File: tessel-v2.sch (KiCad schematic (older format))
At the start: 0 parts

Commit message: io pins, jtag, cortex, high level pins
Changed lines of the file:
@@
 $EndSheet
 $Sheet
-S 6950 5000 2050 3550
+S 6950 5000 2050 4300
 U 548CB7C3
 F0 "I/O" 60
@@
 F9 "MT_WP" I L 6950 5600 60
 F10 "MT_HOLD" I L 6950 5700 60
-F11 "M1_SCL" I R 9000 6200 60
-F12 "M1_SDA" I R 9000 6300 60
-F13 "M1_CLK" I R 9000 6400 60
-F14 "M1_MISO" I R 9000 6500 60
-F15 "M1_MOSI" I R 9000 6600 60
-F16 "M1_G1/TX" I R 9000 6700 60
-F17 "M1_G2/RX" I R 9000 6800 60
-F18 "M1_G3" I R 9000 6900 60
-F19 "M2_SCL" I R 9000 7100 60
-F20 "M2_SDA" I R 9000 7200 60
-F21 "M2_CLK" I R 9000 7300 60
-F22 "M2_MISO" I R 9000 7400 60
-F23 "M2_MOSI" I R 9000 7500 60
-F24 "M2_G1/TX" I R 9000 7600 60
-F25 "M2_G2/RX" I R 9000 7700 60
-F26 "M2_G3" I R 9000 7800 60
-F27 "MT_SCL" I R 9000 5950 60
-F28 "MT_SDA" I R 9000 6050 60
+F11 "MT_SCL" I R 9000 5950 60
+F12 "MT_SDA" I R 9000 6050 60
+F13 "PORTA_SCL" I R 9000 6200 60
+F14 "PORTA_SDA" I R 9000 6300 60
+F15 "PORTA_CLK" I R 9000 6400 60
+F16 "PORTA_MISO" I R 9000 6500 60
+F17 "PORTA_MOSI" I R 9000 6600 60
+F18 "PORTA_G1/TX" I R 9000 6700 60
+F19 "PORTA_G2/RX" I R 9000 6800 60
+F20 "PORTA_G3" I R 9000 6900 60
+F21 "PORTB_SCL" I R 9000 7100 60
+F22 "PORTB_SDA" I R 9000 7200 60
+F23 "PORTB_CLK" I R 9000 7300 60
+F24 "PORTB_MISO" I R 9000 7400 60
+F25 "PORTB_MOSI" I R 9000 7500 60
+F26 "PORTB_G1/TX" I R 9000 7600 60
+F27 "PORTB_G2/RX" I R 9000 7700 60
+F28 "PORTB_G3" I R 9000 7800 60
+F29 "SAM_USB_DP" I R 9000 8000 60
+F30 "SAM_USB_DM" I R 9000 8100 60
+F31 "SWDIO" I R 9000 8250 60
+F32 "SWCLK" I R 9000 8350 60
+F33 "SAM_~RESET" I R 9000 8450 60
+F34 "MT_TWS" I L 6950 5950 60
+F35 "MT_~RESET" I L 6950 6050 60
+F36 "MT_TCLK" I L 6950 6150 60
+F37 "MT_TDO" I L 6950 6250 60
+F38 "MT_TDI" I L 6950 6350 60
+F39 "MT_RTCH" I L 6950 6450 60
 $EndSheet
+Wire Wire Line
+	9000 5150 10800 5150
+Wire Wire Line
+	10800 5150 10800 3650
+Wire Wire Line
+	10800 3650 13150 3650
+Wire Wire Line
+	9000 5250 10900 5250
+Wire Wire Line
+	10900 5250 10900 3750
+Wire Wire Line
+	10900 3750 13150 3750
+Wire Wire Line
+	9000 5500 10700 5500
+Wire Wire Line
+	10700 5500 10700 3050
+Wire Wire Line
+	10700 3050 13150 3050
+Wire Wire Line
+	9000 5600 10600 5600
+Wire Wire Line
+	10600 5600 10600 2850
+Wire Wire Line
+	10600 2850 13150 2850
+Wire Wire Line
+	9000 5700 10500 5700
+Wire Wire Line
+	10500 5700 10500 2950
+Wire Wire Line
+	10500 2950 13150 2950
+Wire Wire Line
+	9000 5800 10400 5800
+Wire Wire Line
+	10400 5800 10400 3150
+Wire Wire Line
+	10400 3150 13150 3150
+Wire Wire Line
+	9000 5950 10300 5950
+Wire Wire Line
+	10300 5950 10300 3450
+Wire Wire Line
+	10300 3450 13150 3450
+Wire Wire Line
+	9000 6050 10200 6050
+Wire Wire Line
+	10200 6050 10200 3350
+Wire Wire Line
+	10200 3350 13150 3350
+Wire Wire Line
+	9000 6200 13000 6200
+Wire Wire Line
+	13000 6200 13000 5350
+Wire Wire Line
+	13000 5350 13150 5350
+Wire Wire Line
+	9000 6300 12900 6300
+Wire Wire Line
+	12900 6300 12900 5250
+Wire Wire Line
+	12900 5250 13150 5250
+Wire Wire Line
+	9000 6400 12800 6400
+Wire Wire Line
+	12800 6400 12800 4850
+Wire Wire Line
+	12800 4850 13150 4850
+Wire Wire Line
+	9000 6500 12700 6500
+Wire Wire Line
+	12700 6500 12700 5050
+Wire Wire Line
+	12700 5050 13150 5050
+Wire Wire Line
+	9000 6600 12600 6600
+Wire Wire Line
+	12600 6600 12600 4750
+Wire Wire Line
+	12600 4750 13150 4750
+Wire Wire Line
+	9000 6700 12500 6700
+Wire Wire Line
+	12500 6700 12500 5550
+Wire Wire Line
+	12500 5550 13150 5550
+Wire Wire Line
+	9000 6800 12400 6800
+Wire Wire Line
+	12400 6800 12400 5650
+Wire Wire Line
+	12400 5650 13150 5650
+Wire Wire Line
+	9000 6900 12300 6900
+Wire Wire Line
+	12300 6900 12300 4100
+Wire Wire Line
+	12300 4100 13150 4100
+Wire Wire Line
+	9000 7100 13000 7100
+Wire Wire Line
+	13000 7100 13000 7750
+Wire Wire Line
+	13000 7750 13150 7750
+Wire Wire Line
+	9000 7200 12900 7200
+Wire Wire Line
+	12900 7200 12900 7650
+Wire Wire Line
+	12900 7650 13150 7650
+Wire Wire Line
+	9000 7300 12800 7300
+Wire Wire Line
+	12800 7300 12800 7350
+Wire Wire Line
+	12800 7350 13150 7350
+Wire Wire Line
+	9000 7400 12750 7400
+Wire Wire Line
+	12750 7400 12750 7150
+Wire Wire Line
+	12750 7150 13150 7150
+Wire Wire Line
+	9000 7500 12450 7500
+Wire Wire Line
+	12450 7500 12450 7250
+Wire Wire Line
+	12450 7250 13150 7250
+Wire Wire Line
+	9000 7600 12750 7600
+Wire Wire Line
+	12750 7600 12750 7950
+Wire Wire Line
+	12750 7950 13150 7950
+Wire Wire Line
+	9000 7700 12650 7700
+Wire Wire Line
+	12650 7700 12650 8050
+Wire Wire Line
+	12650 8050 13150 8050
+Wire Wire Line
+	9000 7800 12000 7800
+Wire Wire Line
+	12000 7800 12000 4200
+Wire Wire Line
+	12000 4200 13150 4200
+Wire Wire Line
+	4500 4150 9450 4150
+Wire Wire Line
+	9450 4150 9450 5500
+Connection ~ 9450 5500
+Wire Wire Line
+	4500 4250 9550 4250
+Wire Wire Line
+	9550 4250 9550 5600
+Connection ~ 9550 5600
+Wire Wire Line
+	4500 4350 9650 4350
+Wire Wire Line
+	9650 4350 9650 5700
+Connection ~ 9650 5700
+Wire Wire Line
+	4500 4450 6850 4450
+Wire Wire Line
+	6850 4450 6850 5600
+Wire Wire Line
+	6850 5600 6950 5600
+Wire Wire Line
+	4500 4550 6750 4550
+Wire Wire Line
+	6750 4550 6750 5700
+Wire Wire Line
+	6750 5700 6950 5700
+Wire Wire Line
+	4500 4650 6650 4650
+Wire Wire Line
+	6650 4650 6650 5500
+Wire Wire Line
+	6650 5500 6950 5500
 $Sheet
-S 13150 2700 2100 5500
+S 13150 2700 2100 6150
 U 548CB895
 F0 "COPROCESSOR" 60
@@
 F38 "GPIO_2_DAC" I L 13150 7050 60
 $EndSheet
-Wire Wire Line
-	9000 5150 10800 5150
-Wire Wire Line
-	10800 5150 10800 3650
-Wire Wire Line
-	10800 3650 13150 3650
-Wire Wire Line
-	9000 5250 10900 5250
-Wire Wire Line
-	10900 5250 10900 3750
-Wire Wire Line
-	10900 3750 13150 3750
-Wire Wire Line
-	9000 5500 10700 5500
-Wire Wire Line
-	10700 5500 10700 3050
-Wire Wire Line
-	10700 3050 13150 3050
-Wire Wire Line
-	9000 5600 10600 5600
-Wire Wire Line
-	10600 5600 10600 2850
-Wire Wire Line
-	10600 2850 13150 2850
-Wire Wire Line
-	9000 5700 10500 5700
-Wire Wire Line
-	10500 5700 10500 2950
-Wire Wire Line
-	10500 2950 13150 2950
-Wire Wire Line
-	9000 5800 10400 5800
-Wire Wire Line
-	10400 5800 10400 3150
-Wire Wire Line
-	10400 3150 13150 3150
-Wire Wire Line
-	9000 5950 10300 5950
-Wire Wire Line
-	10300 5950 10300 3450
-Wire Wire Line
-	10300 3450 13150 3450
-Wire Wire Line
-	9000 6050 10200 6050
-Wire Wire Line
-	10200 6050 10200 3350
-Wire Wire Line
-	10200 3350 13150 3350
-Wire Wire Line
-	9000 6200 13000 6200
-Wire Wire Line
-	13000 6200 13000 5350
-Wire Wire Line
-	13000 5350 13150 5350
-Wire Wire Line
-	9000 6300 12900 6300
-Wire Wire Line
-	12900 6300 12900 5250
-Wire Wire Line
-	12900 5250 13150 5250
-Wire Wire Line
-	9000 6400 12800 6400
-Wire Wire Line
-	12800 6400 12800 4850
-Wire Wire Line
-	12800 4850 13150 4850
-Wire Wire Line
-	9000 6500 12700 6500
-Wire Wire Line
-	12700 6500 12700 5050
-Wire Wire Line
-	12700 5050 13150 5050
-Wire Wire Line
-	9000 6600 12600 6600
-Wire Wire Line
-	12600 6600 12600 4750
-Wire Wire Line
-	12600 4750 13150 4750
-Wire Wire Line
-	9000 6700 12500 6700
-Wire Wire Line
-	12500 6700 12500 5550
-Wire Wire Line
-	12500 5550 13150 5550
-Wire Wire Line
-	9000 6800 12400 6800
-Wire Wire Line
-	12400 6800 12400 5650
-Wire Wire Line
-	12400 5650 13150 5650
-Wire Wire Line
-	9000 6900 12300 6900
-Wire Wire Line
-	12300 6900 12300 4100
-Wire Wire Line
-	12300 4100 13150 4100
-Wire Wire Line
-	9000 7100 13000 7100
-Wire Wire Line
-	13000 7100 13000 7750
-Wire Wire Line
-	13000 7750 13150 7750
-Wire Wire Line
-	9000 7200 12900 7200
-Wire Wire Line
-	12900 7200 12900 7650
-Wire Wire Line
-	12900 7650 13150 7650
-Wire Wire Line
-	9000 7300 12800 7300
-Wire Wire Line
-	12800 7300 12800 7350
-Wire Wire Line
-	12800 7350 13150 7350
-Wire Wire Line
-	9000 7400 12750 7400
-Wire Wire Line
-	12750 7400 12750 7150
-Wire Wire Line
-	12750 7150 13150 7150
-Wire Wire Line
-	9000 7500 12450 7500
-Wire Wire Line
-	12450 7500 12450 7250
-Wire Wire Line
-	12450 7250 13150 7250
-Wire Wire Line
-	9000 7600 12750 7600
-Wire Wire Line
-	12750 7600 12750 7950
-Wire Wire Line
-	12750 7950 13150 7950
-Wire Wire Line
-	9000 7700 12650 7700
-Wire Wire Line
-	12650 7700 12650 8050
-Wire Wire Line
-	12650 8050 13150 8050
-Wire Wire Line
-	9000 7800 12000 7800
-Wire Wire Line
-	12000 7800 12000 4200
-Wire Wire Line
-	12000 4200 13150 4200
-Wire Wire Line
-	4500 4150 9450 4150
-Wire Wire Line
-	9450 4150 9450 5500
-Connection ~ 9450 5500
-Wire Wire Line
-	4500 4250 9550 4250
-Wire Wire Line
-	9550 4250 9550 5600
-Connection ~ 9550 5600
-Wire Wire Line
-	4500 4350 9650 4350
-Wire Wire Line
-	9650 4350 9650 5700
-Connection ~ 9650 5700
-Wire Wire Line
-	4500 4450 6850 4450
-Wire Wire Line
-	6850 4450 6850 5600
-Wire Wire Line
-	6850 5600 6950 5600
-Wire Wire Line
-	4500 4550 6750 4550
-Wire Wire Line
-	6750 4550 6750 5700
-Wire Wire Line
-	6750 5700 6950 5700
-Wire Wire Line
-	4500 4650 6650 4650
-Wire Wire Line
-	6650 4650 6650 5500
-Wire Wire Line
-	6650 5500 6950 5500
 $EndSCHEMATC

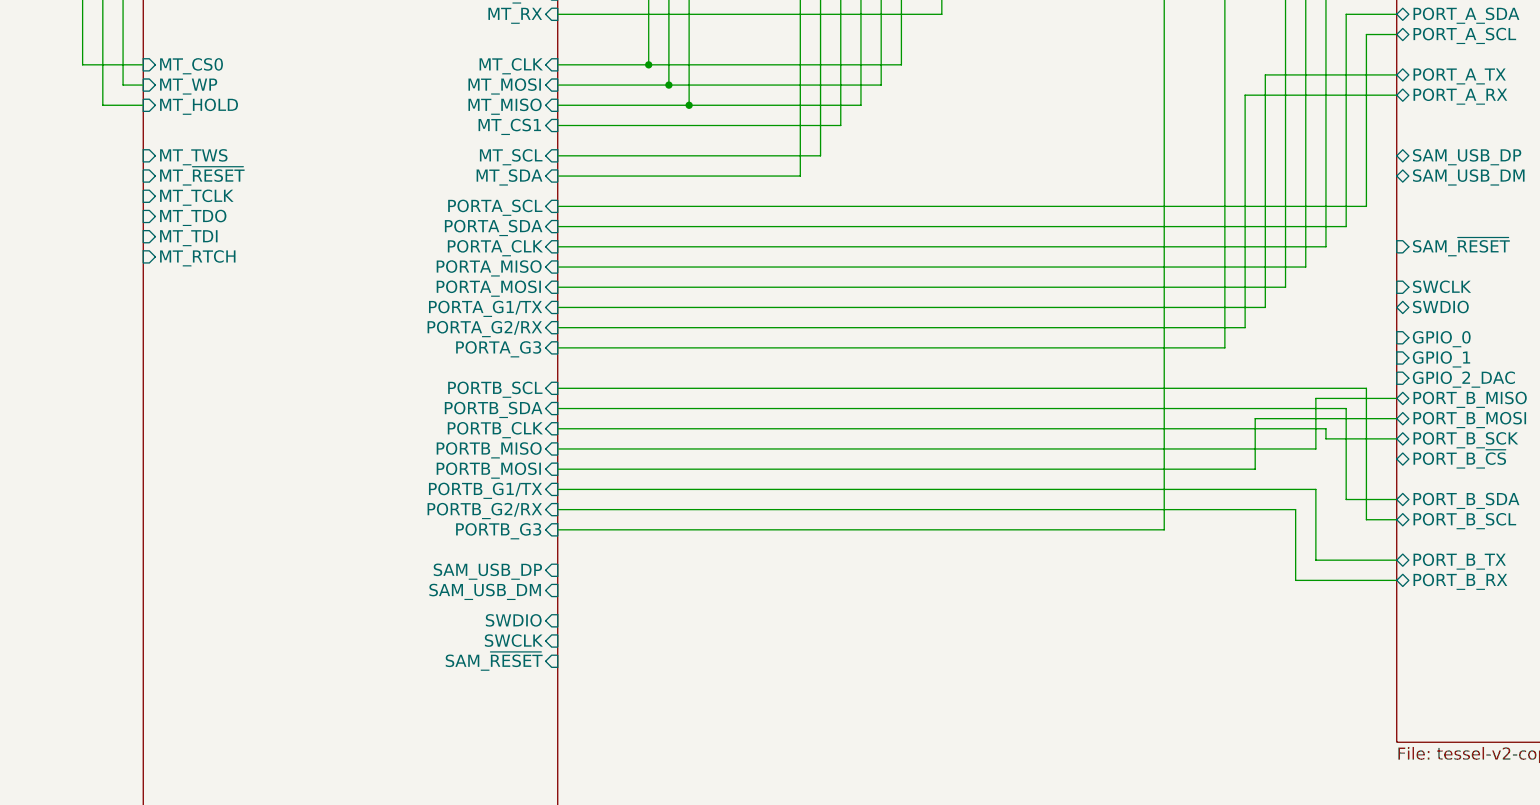
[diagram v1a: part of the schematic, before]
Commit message: wiring up more i/o to cp
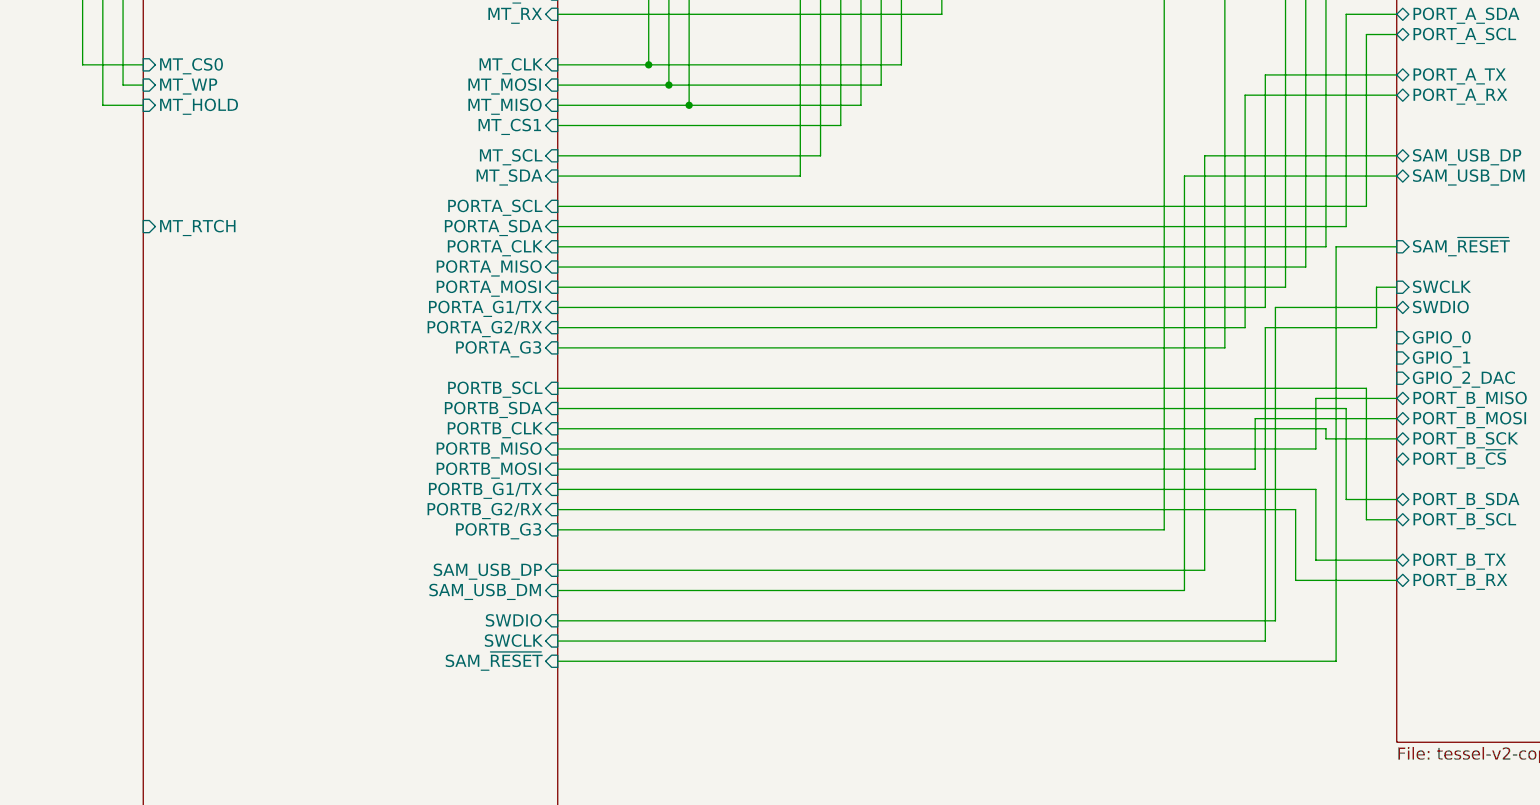
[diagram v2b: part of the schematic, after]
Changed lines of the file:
@@
 F32 "SWCLK" I R 9000 8350 60
 F33 "SAM_~RESET" I R 9000 8450 60
-F34 "MT_TWS" I L 6950 5950 60
-F35 "MT_~RESET" I L 6950 6050 60
-F36 "MT_TCLK" I L 6950 6150 60
-F37 "MT_TDO" I L 6950 6250 60
-F38 "MT_TDI" I L 6950 6350 60
-F39 "MT_RTCH" I L 6950 6450 60
+F34 "MT_RTCH" I L 6950 6300 60
 $EndSheet
 Wire Wire Line
@@
 F38 "GPIO_2_DAC" I L 13150 7050 60
 $EndSheet
+Wire Wire Line
+	9000 8000 12200 8000
+Wire Wire Line
+	12200 8000 12200 5950
+Wire Wire Line
+	12200 5950 13150 5950
+Wire Wire Line
+	9000 8100 12100 8100
+Wire Wire Line
+	12100 8100 12100 6050
+Wire Wire Line
+	12100 6050 13150 6050
+Wire Wire Line
+	9000 8250 12550 8250
+Wire Wire Line
+	12550 8250 12550 6700
+Wire Wire Line
+	12550 6700 13150 6700
+Wire Wire Line
+	9000 8350 12500 8350
+Wire Wire Line
+	12500 8350 12500 6800
+Wire Wire Line
+	12500 6800 13050 6800
+Wire Wire Line
+	13050 6800 13050 6600
+Wire Wire Line
+	13050 6600 13150 6600
+Wire Wire Line
+	9000 8450 12850 8450
+Wire Wire Line
+	12850 8450 12850 6400
+Wire Wire Line
+	12850 6400 13150 6400
 $EndSCHEMATC

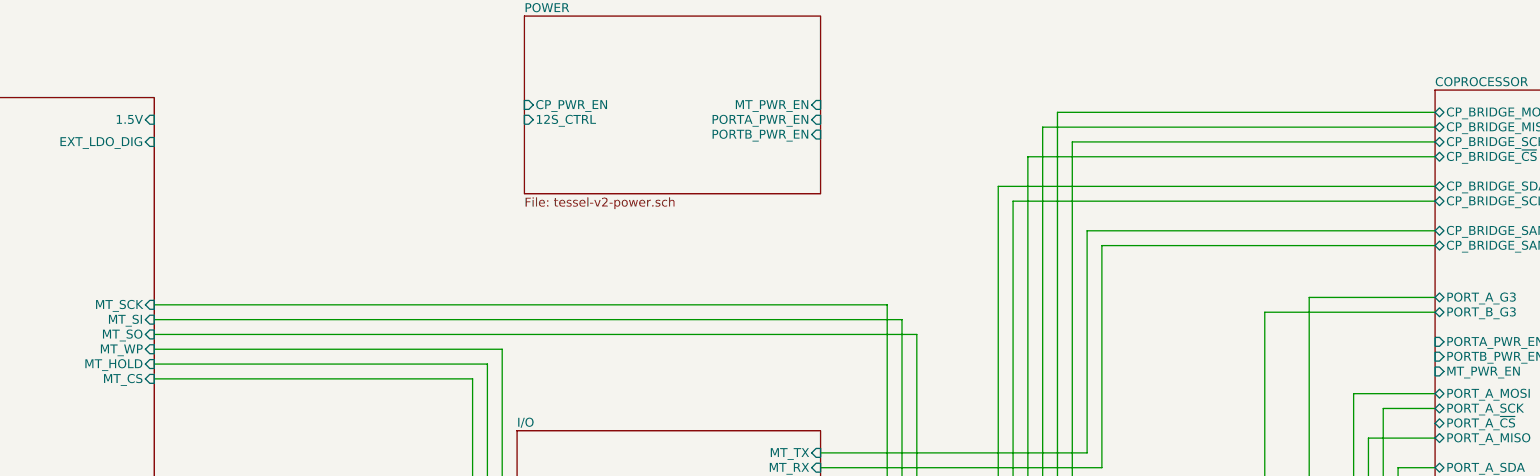
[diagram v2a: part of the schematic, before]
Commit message: setting default boot pins on rf
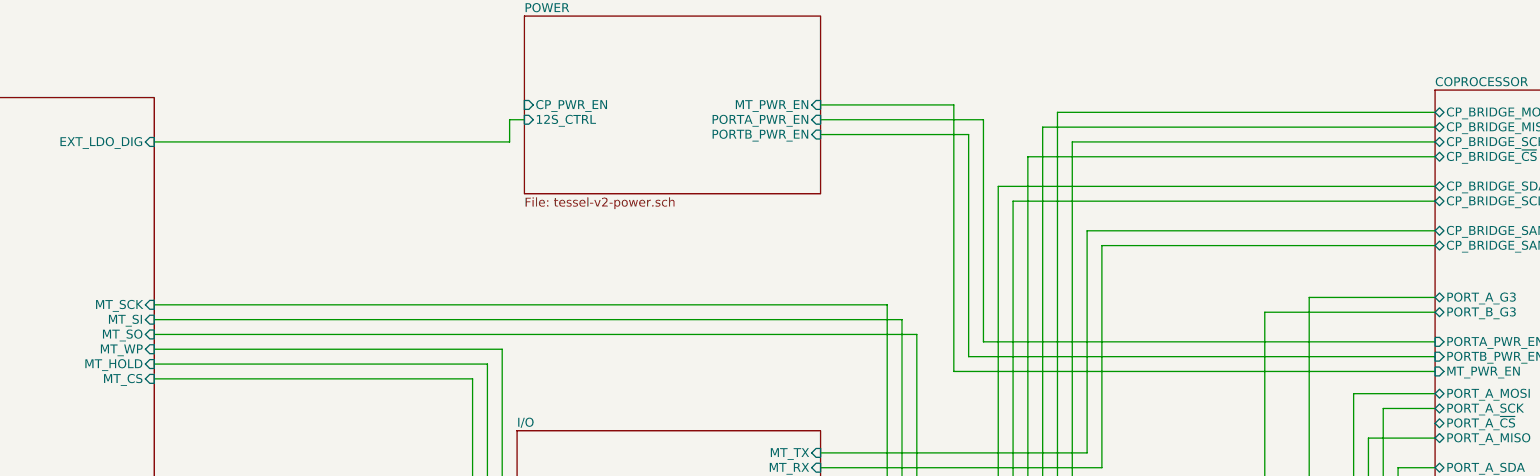
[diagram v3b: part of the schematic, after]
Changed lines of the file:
@@
 F0 "MEDIATEK" 60
 F1 "tessel-v2-mediatek.sch" 60
-F2 "1.5V" I R 4500 2900 60
-F3 "EXT_LDO_DIG" I R 4500 3050 60
-F4 "MT_SI" I R 4500 4250 60
-F5 "MT_SO" I R 4500 4350 60
-F6 "MT_WP" I R 4500 4450 60
-F7 "MT_HOLD" I R 4500 4550 60
-F8 "MT_CS" I R 4500 4650 60
-F9 "MT_SCK" I R 4500 4150 60
+F2 "EXT_LDO_DIG" I R 4500 3050 60
+F3 "MT_SI" I R 4500 4250 60
+F4 "MT_SO" I R 4500 4350 60
+F5 "MT_WP" I R 4500 4450 60
+F6 "MT_HOLD" I R 4500 4550 60
+F7 "MT_CS" I R 4500 4650 60
+F8 "MT_SCK" I R 4500 4150 60
 $EndSheet
 $Sheet
@@
 Wire Wire Line
 	12850 6400 13150 6400
+Wire Wire Line
+	4500 3050 6900 3050
+Wire Wire Line
+	6900 3050 6900 2900
+Wire Wire Line
+	6900 2900 7000 2900
+Wire Wire Line
+	9000 2900 10100 2900
+Wire Wire Line
+	10100 2900 10100 4400
+Wire Wire Line
+	10100 4400 13150 4400
+Wire Wire Line
+	13150 4500 10000 4500
+Wire Wire Line
+	10000 4500 10000 3000
+Wire Wire Line
+	10000 3000 9000 3000
+Wire Wire Line
+	9000 2800 9900 2800
+Wire Wire Line
+	9900 2800 9900 4600
+Wire Wire Line
+	9900 4600 13150 4600
 $EndSCHEMATC

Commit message: second pass schem check
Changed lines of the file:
@@
 F6 "PORTB_PWR_EN" I R 9000 3000 60
-$EndSheet
-$Sheet
-S 6950 5000 2050 4300
-U 548CB7C3
-F0 "I/O" 60
-F1 "tessel-v2-io.sch" 60
-F2 "MT_TX" I R 9000 5150 60
-F3 "MT_RX" I R 9000 5250 60
-F4 "MT_CS0" I L 6950 5500 60
-F5 "MT_CS1" I R 9000 5800 60
-F6 "MT_CLK" I R 9000 5500 60
-F7 "MT_MOSI" I R 9000 5600 60
-F8 "MT_MISO" I R 9000 5700 60
-F9 "MT_WP" I L 6950 5600 60
-F10 "MT_HOLD" I L 6950 5700 60
-F11 "MT_SCL" I R 9000 5950 60
-F12 "MT_SDA" I R 9000 6050 60
-F13 "PORTA_SCL" I R 9000 6200 60
-F14 "PORTA_SDA" I R 9000 6300 60
-F15 "PORTA_CLK" I R 9000 6400 60
-F16 "PORTA_MISO" I R 9000 6500 60
-F17 "PORTA_MOSI" I R 9000 6600 60
-F18 "PORTA_G1/TX" I R 9000 6700 60
-F19 "PORTA_G2/RX" I R 9000 6800 60
-F20 "PORTA_G3" I R 9000 6900 60
-F21 "PORTB_SCL" I R 9000 7100 60
-F22 "PORTB_SDA" I R 9000 7200 60
-F23 "PORTB_CLK" I R 9000 7300 60
-F24 "PORTB_MISO" I R 9000 7400 60
-F25 "PORTB_MOSI" I R 9000 7500 60
-F26 "PORTB_G1/TX" I R 9000 7600 60
-F27 "PORTB_G2/RX" I R 9000 7700 60
-F28 "PORTB_G3" I R 9000 7800 60
-F29 "SAM_USB_DP" I R 9000 8000 60
-F30 "SAM_USB_DM" I R 9000 8100 60
-F31 "SWDIO" I R 9000 8250 60
-F32 "SWCLK" I R 9000 8350 60
-F33 "SAM_~RESET" I R 9000 8450 60
-F34 "MT_RTCH" I L 6950 6300 60
 $EndSheet
 Wire Wire Line
@@
 Wire Wire Line
 	9900 4600 13150 4600
+$Sheet
+S 6950 5000 2050 4300
+U 548CB7C3
+F0 "I/O" 60
+F1 "tessel-v2-io.sch" 60
+F2 "MT_TX" I R 9000 5150 60
+F3 "MT_RX" I R 9000 5250 60
+F4 "MT_CS0" I L 6950 5500 60
+F5 "MT_CS1" I R 9000 5800 60
+F6 "MT_CLK" I R 9000 5500 60
+F7 "MT_MOSI" I R 9000 5600 60
+F8 "MT_MISO" I R 9000 5700 60
+F9 "MT_WP" I L 6950 5600 60
+F10 "MT_HOLD" I L 6950 5700 60
+F11 "MT_SCL" I R 9000 5950 60
+F12 "MT_SDA" I R 9000 6050 60
+F13 "PORTA_SCL" I R 9000 6200 60
+F14 "PORTA_SDA" I R 9000 6300 60
+F15 "PORTA_CLK" I R 9000 6400 60
+F16 "PORTA_MISO" I R 9000 6500 60
+F17 "PORTA_MOSI" I R 9000 6600 60
+F18 "PORTA_G1/TX" I R 9000 6700 60
+F19 "PORTA_G2/RX" I R 9000 6800 60
+F20 "PORTA_G3" I R 9000 6900 60
+F21 "PORTB_SCL" I R 9000 7100 60
+F22 "PORTB_SDA" I R 9000 7200 60
+F23 "PORTB_CLK" I R 9000 7300 60
+F24 "PORTB_MISO" I R 9000 7400 60
+F25 "PORTB_MOSI" I R 9000 7500 60
+F26 "PORTB_G1/TX" I R 9000 7600 60
+F27 "PORTB_G2/RX" I R 9000 7700 60
+F28 "PORTB_G3" I R 9000 7800 60
+F29 "SAM_USB_DP" I R 9000 8000 60
+F30 "SAM_USB_DM" I R 9000 8100 60
+F31 "SWDIO" I R 9000 8250 60
+F32 "SWCLK" I R 9000 8350 60
+F33 "SAM_~RESET" I R 9000 8450 60
+F34 "MT_RTCH" I L 6950 6300 60
+F37 "GPIO0" I R 9000 8900 60
+F38 "GPIO1" I R 9000 9000 60
+F39 "DAC" I R 9000 9100 60
+F40 "PA_CS" I R 9000 8800 60
+F41 "PB_CS" I R 9000 8700 60
+$EndSheet
+Wire Wire Line
+	13150 6850 13000 6850
+Wire Wire Line
+	13000 6850 13000 6950
+Wire Wire Line
+	13000 6950 10500 6950
+Wire Wire Line
+	10500 6950 10500 8900
+Wire Wire Line
+	10500 8900 9000 8900
+Wire Wire Line
+	9000 9000 10550 9000
+Wire Wire Line
+	10550 9000 10550 7000
+Wire Wire Line
+	10550 7000 13050 7000
+Wire Wire Line
+	13050 7000 13050 6950
+Wire Wire Line
+	13050 6950 13150 6950
+Wire Wire Line
+	10600 7050 13150 7050
+Wire Wire Line
+	10600 7050 10600 9100
+Wire Wire Line
+	10600 9100 9000 9100
+Wire Wire Line
+	9000 8800 11550 8800
+Wire Wire Line
+	11550 8800 11550 4950
+Wire Wire Line
+	11550 4950 13150 4950
+Wire Wire Line
+	13150 4950 13150 7450
+Wire Wire Line
+	13050 7450 13050 8700
+Wire Wire Line
+	13050 8700 9000 8700
+Wire Wire Line
+	13150 7450 13050 7450
 $EndSCHEMATC
